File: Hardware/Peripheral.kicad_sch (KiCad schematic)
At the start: 0 parts

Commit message: 11/17 progress update
finished the board, now just need to add the peripheral
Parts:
- added J1: 2x40 Header, Connector_PinHeader_2.54mm:PinHeader_2x20_P2.54mm_Vertical, symbol Connector_Generic:Conn_02x20_Odd_Even
- added Jr1: HDMI_A, Sync_VT extras:CNC_2001-1-2-21-00-BK, symbol Connector:HDMI_A
- added MK1: SPH0645LM4H, Sensor_Audio:Knowles_SPH0645LM4H-6_3.5x2.65mm, symbol Sensor_Audio:SPH0645LM4H
- added Q1, Q2: BSS138, Package_TO_SOT_SMD:SOT-23, symbol Transistor_FET:BSS138
- added R29, R30, R31, R32: 10k, Capacitor_SMD:C_0402_1005Metric, symbol Device:R
- added R33, R34: 100k, Resistor_SMD:R_0402_1005Metric_Pad0.72x0.64mm_HandSolder, symbol Device:R
- added RN1: R_Pack08, Resistor_SMD:R_Array_Convex_8x0602, symbol Device:R_Pack08
- added U11: ICM-20948, Sensor_Motion:InvenSense_QFN-24_3x3mm_P0.4mm, symbol Sensor_Motion:ICM-20948
- added U12: MS5611-01BA, Package_LGA:LGA-8_3x5mm_P1.25mm, symbol Sensor_Pressure:MS5611-01BA
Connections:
- new net: U12.4 (CSB), U12.5 (CSB)
- new net: Q1.2 (S), R29.1
- new net: R33.2, R34.1
- new net: U11.18 (GND), U11.20 (GND)
- new net: Jr1.19 (HPD), R34.2
- new net: Jr1.1 (D2+), RN1.16 (R1.2)
- new net: Jr1.10 (CK+), RN1.10 (R7.2)
- new net: Jr1.12 (CK-), RN1.9 (R8.2)
- new net: Jr1.3 (D2-), RN1.15 (R2.2)
- new net: Jr1.4 (D1+), RN1.14 (R3.2)
- new net: Jr1.6 (D1-), RN1.13 (R4.2)
- new net: Jr1.7 (D0+), RN1.12 (R5.2)
- new net: Jr1.9 (D0-), RN1.11 (R6.2)
- new net: Q2.2 (S), R31.2
- new net +3V3: J1.1 (Pin_1), J1.17 (Pin_17), Q1.1 (G), Q2.1 (G), R29.2, R31.1
- new net +5V: J1.2 (Pin_2), J1.4 (Pin_4), Jr1.18 (+5V), R30.2, R32.1
- new net CK+: RN1.7 (R7.1)
- new net CK-: RN1.8 (R8.1)
- new net D0+: RN1.5 (R5.1)
- new net D0-: RN1.6 (R6.1)
- new net D1+: RN1.3 (R3.1)
- new net D1-: RN1.4 (R4.1)
- new net D2+: RN1.1 (R1.1)
- new net D2-: RN1.2 (R2.1)
- new net GND: J1.14 (Pin_14), J1.20 (Pin_20), J1.25 (Pin_25), J1.30 (Pin_30), J1.34 (Pin_34), J1.39 (Pin_39), J1.6 (Pin_6), J1.9 (Pin_9), Jr1.17 (GND), Jr1.S1 (GND), Jr1.S2 (GND), Jr1.S3 (GND), Jr1.S4 (GND), Jr1.SH, R33.1
- new net GPIO0: J1.3 (Pin_3)
- new net GPIO1: J1.5 (Pin_5)
- new net GPIO10: J1.29 (Pin_29)
- new net GPIO11: J1.31 (Pin_31)
- new net GPIO12: J1.33 (Pin_33)
- new net GPIO13: J1.35 (Pin_35)
- new net GPIO14: J1.37 (Pin_37)
- new net GPIO15: J1.40 (Pin_40)
- new net GPIO16: J1.38 (Pin_38)
- new net GPIO17: J1.36 (Pin_36)
- new net GPIO18: J1.32 (Pin_32)
- new net GPIO19: J1.28 (Pin_28)
- new net GPIO2: J1.7 (Pin_7)
- new net GPIO20: J1.26 (Pin_26)
- new net GPIO21: J1.24 (Pin_24)
- new net GPIO22: J1.22 (Pin_22)
- new net GPIO23: J1.18 (Pin_18)
- new net GPIO24: J1.16 (Pin_16)
- new net GPIO25: J1.12 (Pin_12)
- new net GPIO26: J1.10 (Pin_10)
- new net GPIO27: J1.8 (Pin_8)
- new net GPIO3: J1.11 (Pin_11)
- new net GPIO4: J1.13 (Pin_13)
- new net GPIO5: J1.15 (Pin_15)
- new net GPIO6: J1.19 (Pin_19)
- new net GPIO7: J1.21 (Pin_21)
- new net GPIO8: J1.23 (Pin_23)
- new net GPIO9: J1.27 (Pin_27)
- new net HDMIscl: Jr1.15 (SCL), Q2.3 (D), R32.2
- new net HDMIsda: Jr1.16 (SDA), Q1.3 (D), R30.1
- no-connect marks 0 -> 6
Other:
- note added: "I2C MIO 14-15"
- note added: "SPI1 MIO 34-37"
- note added: "UART0 MIO 10-11"

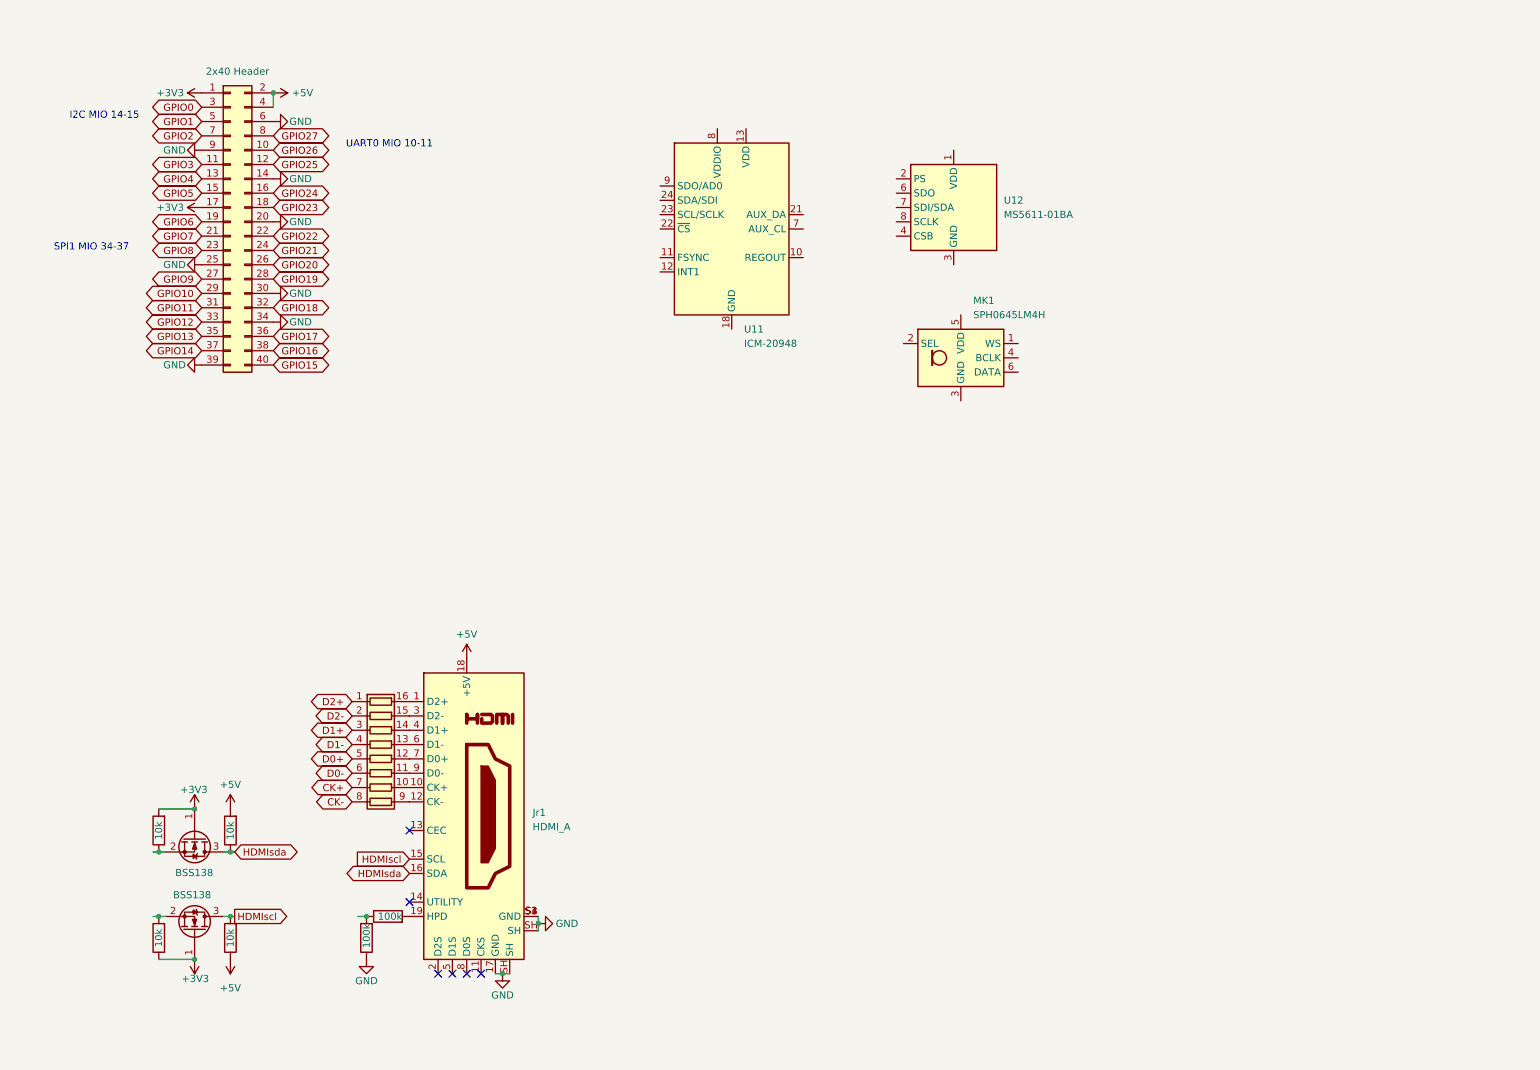
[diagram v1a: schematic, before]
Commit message: 11/19 update
add new header for jtag and fixed a couple of small things
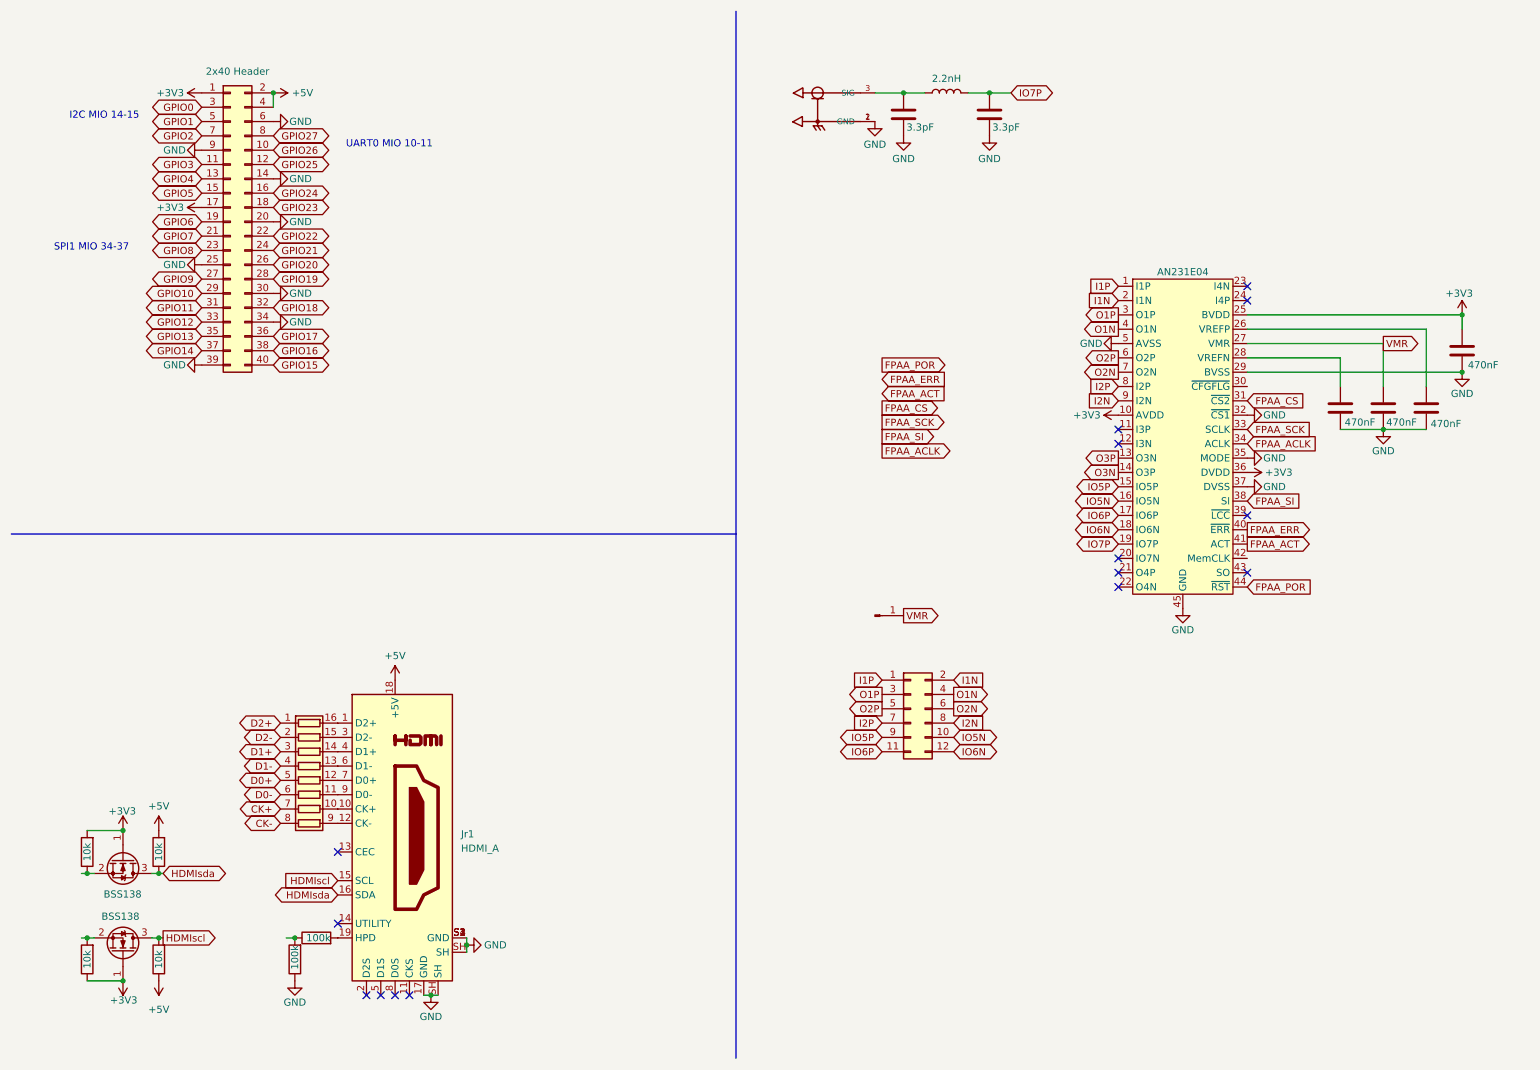
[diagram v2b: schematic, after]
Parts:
- removed MK1: SPH0645LM4H, Sensor_Audio:Knowles_SPH0645LM4H-6_3.5x2.65mm, symbol Sensor_Audio:SPH0645LM4H
- removed U11: ICM-20948, Sensor_Motion:InvenSense_QFN-24_3x3mm_P0.4mm, symbol Sensor_Motion:ICM-20948
- removed U12: MS5611-01BA, Package_LGA:LGA-8_3x5mm_P1.25mm, symbol Sensor_Pressure:MS5611-01BA
- added C29, C30, C31, C32: 470nF, Capacitor_SMD:C_0201_0603Metric, symbol Device:C
- added C33, C34: 3.3pF, Capacitor_SMD:C_0201_0603Metric, symbol Device:C
- added J4: Conn_02x06_Odd_Even_MountingPin, Connector_PinHeader_2.54mm:PinHeader_2x06_P2.54mm_Vertical, symbol Connector_Generic_MountingPin:Conn_02x06_Odd_Even_MountingPin
- added J5: U.FL-R-SMT_01_, Sync_VT extras:HRS_U.FL-R-SMT_01_, symbol Personal:U.FL-R-SMT_01_
- added J6: Conn_01x01_Pin, Connector_PinHeader_2.00mm:PinHeader_1x01_P2.00mm_Vertical, symbol Connector:Conn_01x01_Pin
- added L3: 2.2nH, Inductor_SMD:L_0201_0603Metric, symbol Device:L
- added Ue1: AN231E04, Package_DFN_QFN:QFN-44-1EP_7x7mm_P0.5mm_EP5.2x5.2mm, symbol Personal:AN231
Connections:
- net +3V3: now also C32.1, Ue1.10 (AVDD), Ue1.25 (BVDD), Ue1.36 (DVDD)
- net GND: now also C29.2, C30.2, C31.2, C32.2, C33.2, C34.2, J5.1 (GND), J5.2 (GND), Ue1.29 (BVSS), Ue1.32 (~{CS1}), Ue1.35 (MODE), Ue1.37 (DVSS), Ue1.45 (GND), Ue1.5 (AVSS)
- new net: C31.1, Ue1.26 (VREFP)
- new net: C29.1, Ue1.28 (VREFN)
- new net: C33.1, J5.3 (SIG), L3.1
- new net FPAA_ACLK: Ue1.34 (ACLK)
- new net FPAA_ACT: Ue1.41 (ACT)
- new net FPAA_CS: Ue1.31 (~{CS2})
- new net FPAA_ERR: Ue1.40 (~{ERR})
- new net FPAA_POR: Ue1.44 (~{RST})
- new net FPAA_SCK: Ue1.33 (SCLK)
- new net FPAA_SI: Ue1.38 (SI)
- new net I1N: J4.2 (Pin_2), Ue1.2 (I1N)
- new net I1P: J4.1 (Pin_1), Ue1.1 (I1P)
- new net I2N: J4.8 (Pin_8), Ue1.9 (I2N)
- new net I2P: J4.7 (Pin_7), Ue1.8 (I2P)
- new net IO5N: J4.10 (Pin_10), Ue1.16 (IO5N)
- new net IO5P: J4.9 (Pin_9), Ue1.15 (IO5P)
- new net IO6N: J4.12 (Pin_12), Ue1.18 (IO6N)
- new net IO6P: J4.11 (Pin_11), Ue1.17 (IO6P)
- new net IO7P: C34.1, L3.2, Ue1.19 (IO7P)
- new net O1N: J4.4 (Pin_4), Ue1.4 (O1N)
- new net O1P: J4.3 (Pin_3), Ue1.3 (O1P)
- new net O2N: J4.6 (Pin_6), Ue1.7 (O2N)
- new net O2P: J4.5 (Pin_5), Ue1.6 (O2P)
- new net O3N: Ue1.14 (O3P)
- new net O3P: Ue1.13 (O3N)
- new net VMR: C30.1, J6.1 (Pin_1), Ue1.27 (VMR)
- no-connect marks 6 -> 15
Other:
- moved on the sheet: Jr1

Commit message: 11/21 update
finished annotating the schematic and add pictures and output the pdf
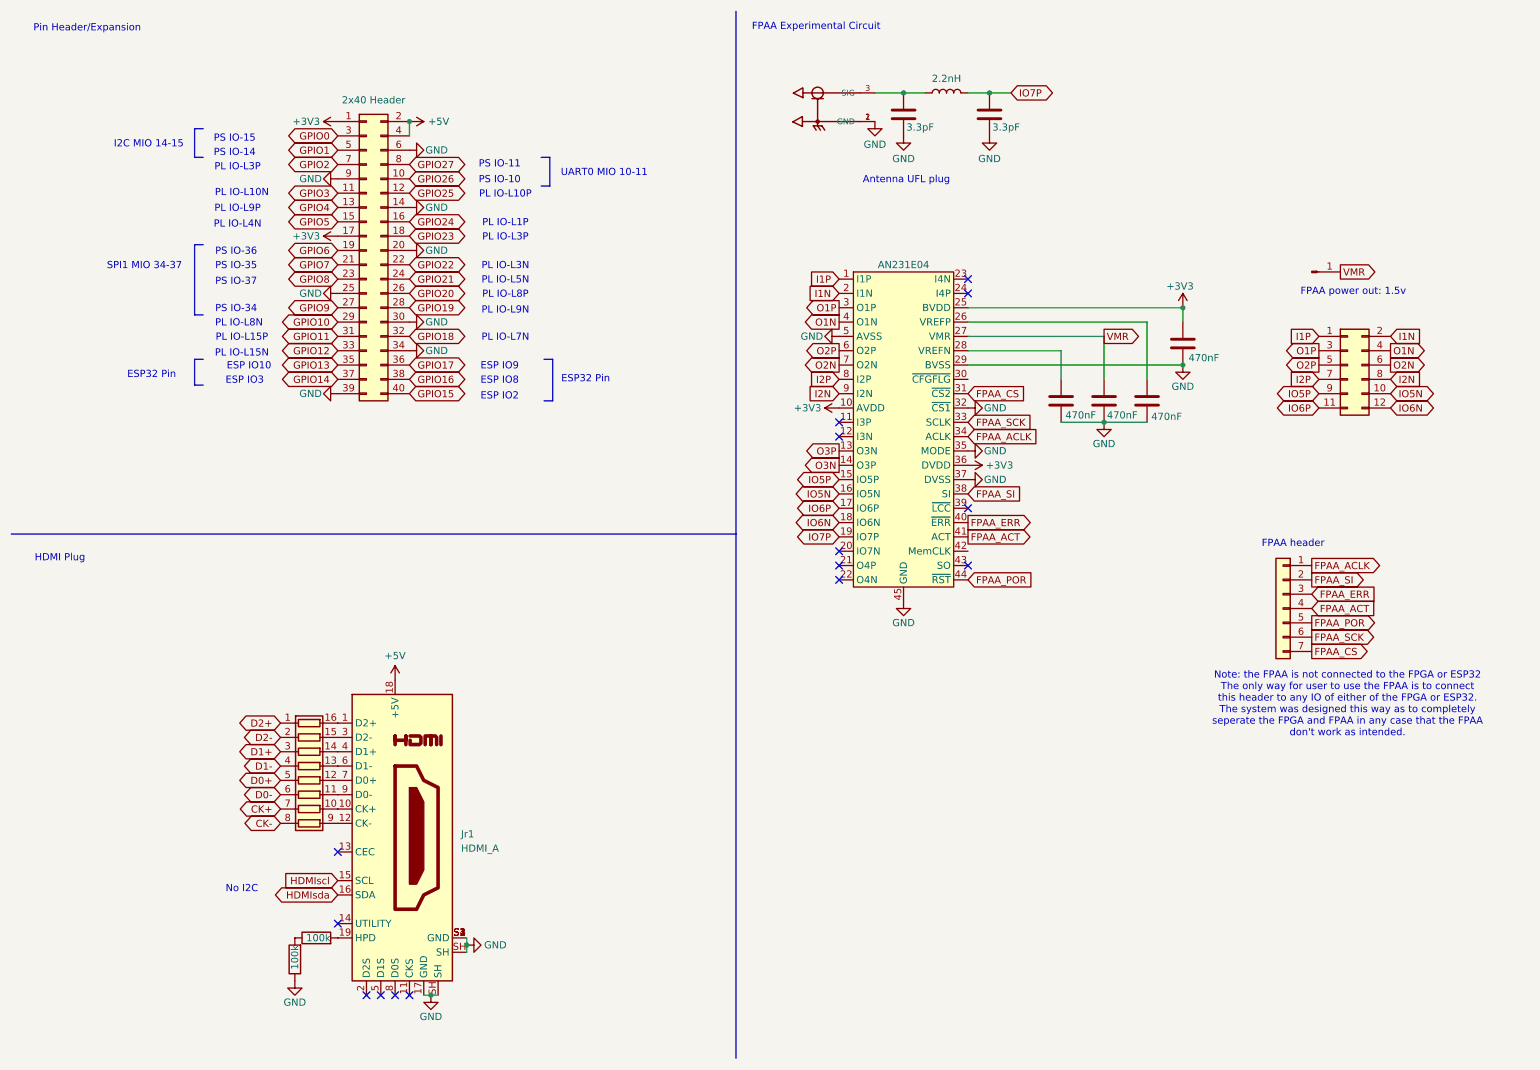
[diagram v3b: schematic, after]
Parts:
- removed Q1, Q2: BSS138, Package_TO_SOT_SMD:SOT-23, symbol Transistor_FET:BSS138
- removed R29, R30, R31, R32: 10k, Capacitor_SMD:C_0402_1005Metric, symbol Device:R
- added J8: Conn_01x07_MountingPin, Connector_PinHeader_1.00mm:PinHeader_1x07_P1.00mm_Vertical, symbol Connector_Generic_MountingPin:Conn_01x07_MountingPin
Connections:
- net FPAA_ACLK: now also J8.1 (Pin_1)
- net FPAA_ACT: now also J8.4 (Pin_4)
- net FPAA_CS: now also J8.7 (Pin_7)
- net FPAA_ERR: now also J8.3 (Pin_3)
- net FPAA_POR: now also J8.5 (Pin_5)
- net FPAA_SCK: now also J8.6 (Pin_6)
- net FPAA_SI: now also J8.2 (Pin_2)
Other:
- note added: "Antenna UFL plug"
- note added: "ESP IO10"
- note added: "ESP IO2"
- note added: "ESP IO3"
- note added: "ESP IO8"
- note added: "ESP IO9"
- note added: "ESP32 Pin"
- note added: "FPAA Experimental Circuit"
- note added: "FPAA header"
- note added: "FPAA power out: 1.5v"
- note added: "HDMI Plug"
- note added: "No I2C"
- note added: "Note: the FPAA is not connected to the FPGA or ESP32 The only way for user to use the FPAA is to connect this header to any IO of either of the FPGA or ESP32. The system was designed this way as to completely seperate the FPGA and FPAA in any case that the FPAA don't work as intended."
- note added: "PL IO-L10N"
- note added: "PL IO-L10P"
- note added: "PL IO-L15N"
- note added: "PL IO-L15P"
- note added: "PL IO-L1P"
- note added: "PL IO-L3N"
- note added: "PL IO-L3P"
- note added: "PL IO-L4N"
- note added: "PL IO-L5N"
- note added: "PL IO-L7N"
- note added: "PL IO-L8N"
- note added: "PL IO-L8P"
- note added: "PL IO-L9N"
- note added: "PL IO-L9P"
- note added: "PS IO-10"
- note added: "PS IO-11"
- note added: "PS IO-14"
- note added: "PS IO-15"
- note added: "PS IO-34"
- note added: "PS IO-35"
- note added: "PS IO-36"
- note added: "PS IO-37"
- note added: "Pin Header/Expansion"
